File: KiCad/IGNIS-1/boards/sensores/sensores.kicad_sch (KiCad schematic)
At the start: 10 parts, among them J41 Backplane_2x10, U20 BME280, U21 MPU6050, U22 MQ-135, U24 GPS NEO-6M

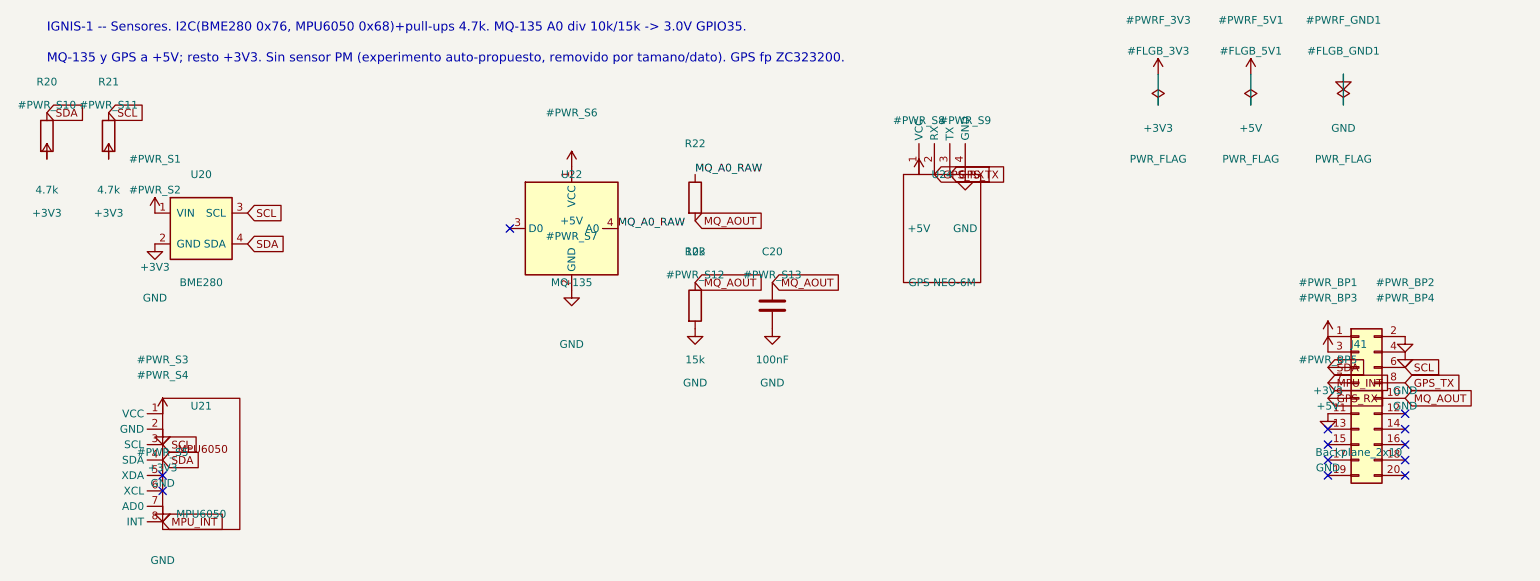
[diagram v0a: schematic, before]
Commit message: Actualizado los boards de IGNIS - separado en 3 boards
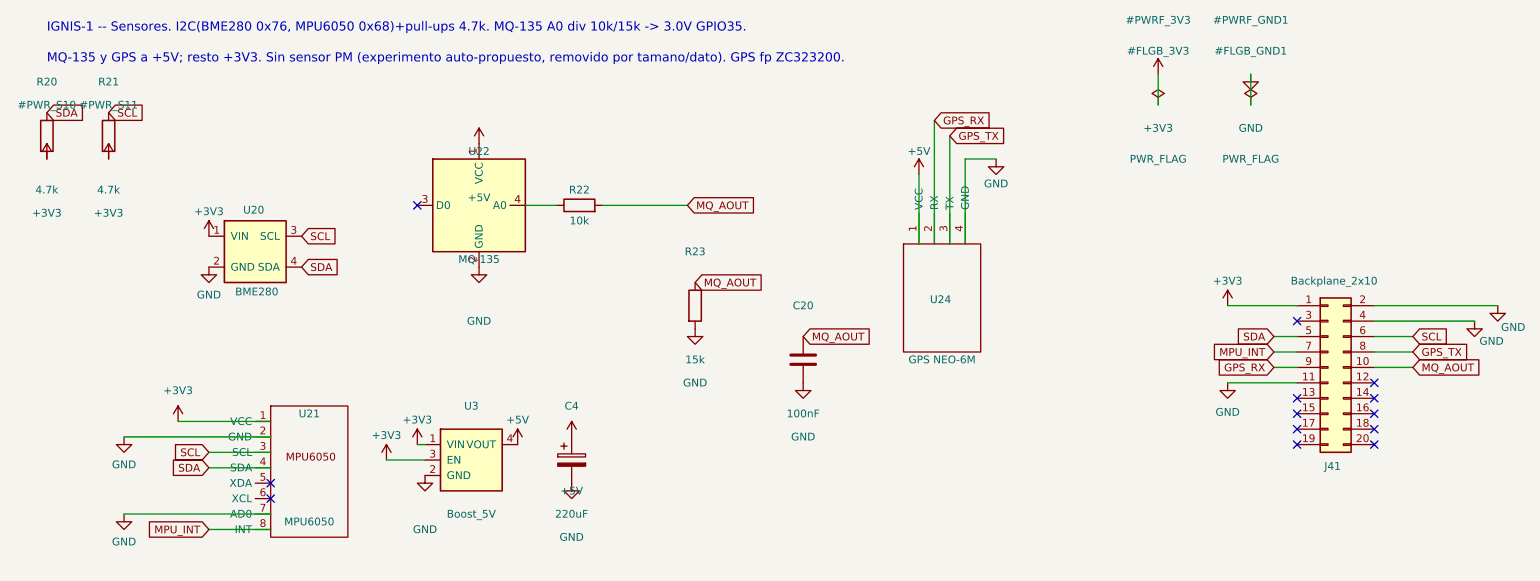
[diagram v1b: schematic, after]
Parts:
- added C4: 220uF, Capacitor_THT:CP_Radial_D6.3mm_P2.50mm, symbol Device:C_Polarized
- added U3: Boost_5V, Connector_PinHeader_2.54mm:PinHeader_1x04_P2.54mm_Vertical, symbol IGNIS1:DCDC_Module
- C20: footprint Capacitor_SMD:C_0805_2012Metric -> Capacitor_SMD:C_0805_2012Metric_Pad1.18x1.45mm_HandSolder
- R20, R21, R22, R23: footprint Resistor_SMD:R_0805_2012Metric -> Resistor_SMD:R_0805_2012Metric_Pad1.20x1.40mm_HandSolder
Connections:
- net +3V3: now also U3.1 (VIN), U3.3 (EN)
- net +5V: now also C4.1, U3.4 (VOUT); no longer J41.3 (Pin_3)
- net GND: now also C4.2, U3.2 (GND)
- net MQ_A0_RAW: no longer names the net of R22.1, U22.4 (A0)
- no-connect marks 12 -> 13
